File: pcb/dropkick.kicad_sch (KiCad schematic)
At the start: 50 parts, among them SW1 450405020524, SW2 KMR211NG_LFS, U1 ATSAMD21G18A-AUT, U2 SAM-M8Q-0-10, U3 MCP73831T-2ACI/OT, U4 DPS310XTSA1, U5 MPU-6050, U6 SPX3819-3.3, X1 microUSB, X2 JSTPH, X3 microsd, X5 32768Hz

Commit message: V3 board
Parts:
- removed JP4: HEADER-1X12, 1X12_ROUND, symbol Adafruit Feather M0 Adalogger-eagle-import:HEADER-1X12
- removed JP5: HEADER-1X16ROUND, 1X16_ROUND, symbol Adafruit Feather M0 Adalogger-eagle-import:HEADER-1X16ROUND
- removed R11: 4.7K, RESPACK_4X0603, symbol Adafruit MPU6050-eagle-import:RESISTOR_4PACK
- removed U2: SAM-M8Q-0-10, MODULE_SAM-M8Q-0-10, symbol dropkick:SAM-M8Q-0-10
- added J1: Conn_01x08, Connector_PinHeader_2.54mm:PinHeader_1x08_P2.54mm_Vertical, symbol Connector_Generic:Conn_01x08
- added R11, R12: 10K, Resistor_SMD:R_0603_1608Metric, symbol Adafruit MPU6050-eagle-import:RESISTOR_0603_NOOUT
- added R4, R5: 0K, Resistor_SMD:R_0603_1608Metric, symbol Adafruit Feather M0 Adalogger-eagle-import:RESISTOR_0603_NOOUT
- added U2: CAM-M8C-0, lib_fr:CAM-M8C-0, symbol dropkick:CAM-M8C-0
- added X4: ANTENNA_U.FL, lib_fr:U.FL, symbol Adafruit Ultimate GPS FeatherWing-eagle-import:ANTENNA_U.FL
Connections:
- net 3.3V is gone; now on net +3V3: C11.1, C6.1, R10.1, SJ4.1, U4.6 (VDDIO), U4.8 (VDD), U5.13 (VDD), U5.8 (VLOGIC)
- net VCC is gone; now on net +3V3: JP2.1
- net +3V3: now also R11.1, R12.1, U2.1 (VCC_IO), U2.9 (VCC)
- net A0: now also J1.6 (Pin_6)
- net A1: now also J1.7 (Pin_7)
- net AREF: now also J1.5 (Pin_5)
- net D0: now also J1.8 (Pin_8)
- net GND: now also J1.4 (Pin_4), U2.10 (GND), U2.11 (GND), U2.12 (GND), U2.13 (GND), U2.14 (GND), U2.15 (GND), U2.18 (GND), U2.19 (GND), U2.21 (GND), U2.22 (GND), U2.27 (GND), U2.31 (GND), U2.4 (GND), U2.5 (GND), X4.1 (GND@0), X4.2 (GND@1)
- net SCL: now also J1.2 (Pin_2), R11.2, U2.6 (SCL/_SPI_CLK)
- net SDA: now also J1.3 (Pin_3), R12.2, U2.3 (SDA/_SPI_CS_N)
- net VBACKUP: now also U2.8 (V_BCKP)
- net VBAT: now also J1.1 (Pin_1)
- new net: R4.2, R5.2, U2.17 (RF_IN)
- new net: R5.1, X4.3 (SIGNAL)
- new net RF: R4.1, U2.16 (RF_OUT)
- no-connect marks 21 -> 26
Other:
- note added: "GNSS RECEIVER - CAM-M8C"
- note removed: "GPS RECEIVER"
- moved on the sheet: B1, C11, TP1

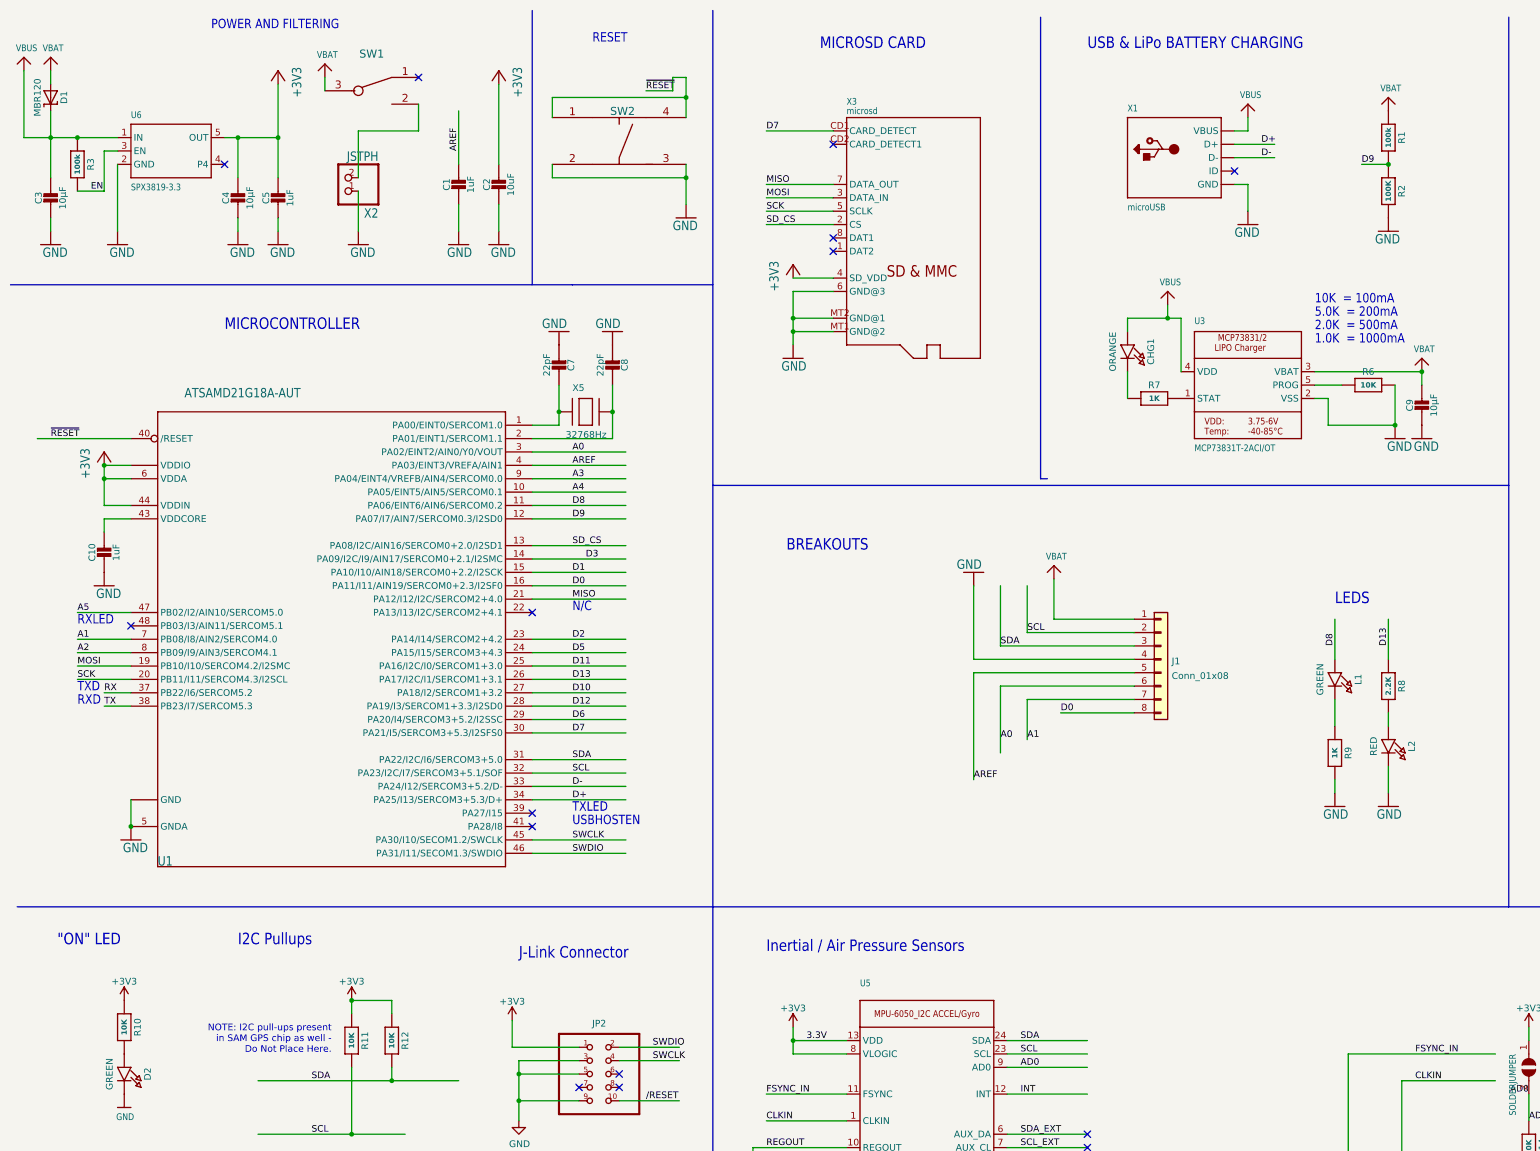
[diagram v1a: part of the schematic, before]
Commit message: Alternate REG IC
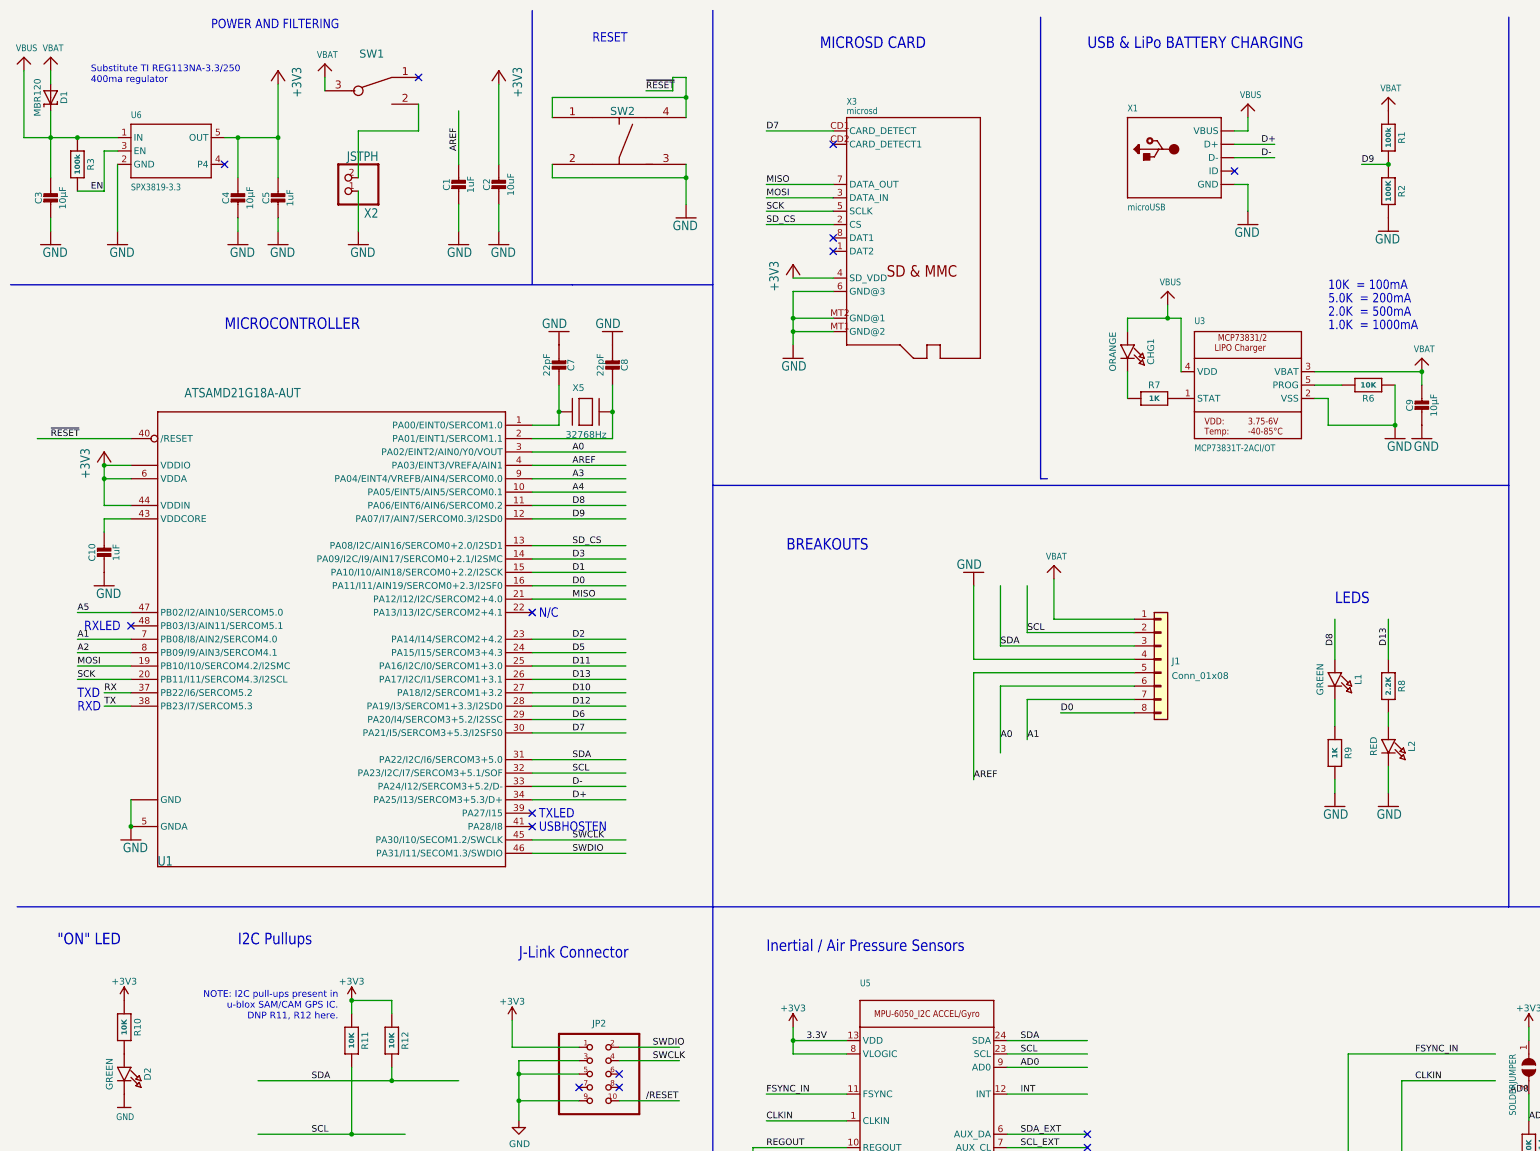
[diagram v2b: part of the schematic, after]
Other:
- note added: "NOTE: I2C pull-ups present in u-blox SAM/CAM GPS IC. DNP R11, R12 here."
- note added: "Substitute TI REG113NA-3.3/250 400ma regulator"
- note removed: "NOTE: I2C pull-ups present in SAM GPS chip as well - Do Not Place Here."
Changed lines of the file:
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@@
     (stroke (width 0) (type default) (color 0 0 0 0))
   )
-  (text "TXLED" (at 121.92 167.64 180)
-    (effects (font (size 1.778 1.5113)) (justify left bottom))
-  )
-  (text "TXD" (at 27.94 144.78 180)
+  (text "TXLED" (at 115.57 168.91 180)
+    (effects (font (size 1.778 1.5113)) (justify left bottom))
+  )
+  (text "TXD" (at 27.94 146.05 180)
     (effects (font (size 1.778 1.5113)) (justify left bottom))
   )
@@
     (effects (font (size 2.1844 1.8567)) (justify left bottom))
   )
-  (text "USBHOSTEN" (at 121.92 170.18 180)
-    (effects (font (size 1.778 1.5113)) (justify left bottom))
-  )
-  (text "RXD" (at 27.94 147.32 180)
-    (effects (font (size 1.778 1.5113)) (justify left bottom))
-  )
-  (text "N/C" (at 121.92 129.54 180)
+  (text "USBHOSTEN" (at 115.57 171.45 180)
+    (effects (font (size 1.778 1.5113)) (justify left bottom))
+  )
+  (text "RXD" (at 27.94 148.59 180)
+    (effects (font (size 1.778 1.5113)) (justify left bottom))
+  )
+  (text "N/C" (at 115.57 130.81 180)
     (effects (font (size 1.778 1.5113)) (justify left bottom))
   )
@@
     (effects (font (size 2.1844 1.8567)) (justify left bottom))
   )
-  (text "10K  = 100mA" (at 262.89 71.12 180)
+  (text "10K  = 100mA" (at 265.43 68.58 180)
     (effects (font (size 1.778 1.5113)) (justify left bottom))
   )
@@
     (effects (font (size 2.1844 1.8567)) (justify left bottom))
   )
-  (text "1.0K  = 1000mA" (at 262.89 78.74 180)
-    (effects (font (size 1.778 1.5113)) (justify left bottom))
-  )
-  (text "5.0K  = 200mA" (at 262.89 73.66 180)
+  (text "1.0K  = 1000mA" (at 265.43 76.2 180)
+    (effects (font (size 1.778 1.5113)) (justify left bottom))
+  )
+  (text "5.0K  = 200mA" (at 265.43 71.12 180)
     (effects (font (size 1.778 1.5113)) (justify left bottom))
   )
@@
     (effects (font (size 2.1844 1.8567)) (justify left bottom))
   )
-  (text "RXLED" (at 27.94 132.08 180)
-    (effects (font (size 1.778 1.5113)) (justify left bottom))
+  (text "RXLED" (at 29.21 133.35 180)
+    (effects (font (size 1.778 1.5113)) (justify left bottom))
+  )
+  (text "Substitute TI REG113NA-3.3/250\n400ma regulator\n" (at 30.48 29.21 0)
+    (effects (font (size 1.27 1.27)) (justify left bottom))
   )
   (text "LEDS" (at 266.7 128.27 180)
     (effects (font (size 2.1844 1.8567)) (justify left bottom))
   )
-  (text "2.0K  = 500mA" (at 262.89 76.2 180)
+  (text "2.0K  = 500mA" (at 265.43 73.66 180)
     (effects (font (size 1.778 1.5113)) (justify left bottom))
   )
@@
     (effects (font (size 2.1844 1.8567)) (justify left bottom))
   )
-  (text "NOTE: I2C pull-ups present\nin SAM GPS chip as well - \nDo Not Place Here."
-    (at 76.2 213.36 0)
+  (text "NOTE: I2C pull-ups present in\nu-blox SAM/CAM GPS IC.\nDNP R11, R12 here."
+    (at 77.47 207.01 0)
     (effects (font (size 1.27 1.27)) (justify right bottom))
   )
-  (label "D3" (at 124.46 119.38 0)
+  (label "D3" (at 121.92 119.38 0)
     (effects (font (size 1.2446 1.2446)) (justify left bottom))
   )
@@
   (symbol (lib_id "Adafruit Feather M0 Adalogger-eagle-import:RESISTOR_0603_NOOUT") (at 273.05 86.36 0) (unit 1)
     (in_bom yes) (on_board yes)
-    (property "Reference" "R6" (id 0) (at 273.05 83.82 0))
+    (property "Reference" "R6" (id 0) (at 273.05 88.9 0))
     (property "Value" "10K" (id 1) (at 273.05 86.36 0)
       (effects (font (size 1.016 1.016) bold))
@@
       (effects (font (size 1.27 1.27)) hide)
     )
-    (property "Datasheet" "" (id 3) (at 250.19 86.36 0)
+    (property "Datasheet" "https://www.mouser.com/datasheet/2/268/MCHP_S_A0010728890_1-2521060.pdf" (id 3) (at 250.19 86.36 0)
       (effects (font (size 1.27 1.27)) hide)
     )
@@
       (effects (font (size 1.27 1.27)) hide)
     )
-    (property "Datasheet" "" (id 3) (at 45.72 41.91 0)
-      (effects (font (size 1.27 1.27)) hide)
-    )
+    (property "Datasheet" "https://assets.maxlinear.com/web/documents/spx3819.pdf" (id 3) (at 45.72 41.91 0)
+      (effects (font (size 1.27 1.27)) hide)
+    )

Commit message: IC substitutions
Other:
- note added: "Sub B0540W-7-F"
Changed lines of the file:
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@@
     (effects (font (size 1.27 1.27)) (justify right bottom))
+  )
+  (text "Sub B0540W-7-F" (at 15.24 44.45 90)
+    (effects (font (size 1.27 1.27)) (justify left bottom))
   )
   (label "D3" (at 121.92 119.38 0)

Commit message: Reorganize footprint libraries
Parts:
- C12, C13: footprint 0603-NO -> Capacitor_SMD:C_0603_1608Metric
- R1, R3: value 100k -> 100K; footprint 0603-NO -> Resistor_SMD:R_0603_1608Metric
- R2: footprint 0603-NO -> Resistor_SMD:R_0603_1608Metric
- SJ4: footprint 310:0603-NO -> Resistor_SMD:R_0603_1608Metric
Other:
- note added: "EXT"
- note added: "INT"
- note added: "Install one of INT (R4) or EXT (R5) jumper"
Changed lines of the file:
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@@
     (stroke (width 0) (type default) (color 0 0 0 0))
+  )
+  (text "Install one of INT (R4) or \nEXT (R5) jumper" (at 325.12 88.9 0)
+    (effects (font (size 1.27 1.27)) (justify left bottom))
   )
   (text "TXLED" (at 115.57 168.91 180)
@@
     (effects (font (size 1.778 1.5113)) (justify left bottom))
   )
+  (text "INT" (at 334.01 93.98 0)
+    (effects (font (size 1.27 1.27)) (justify left bottom))
+  )
   (text "Inertial / Air Pressure Sensors" (at 158.75 194.31 180)
     (effects (font (size 2.1844 1.8567)) (justify left bottom))
@@
   (text "5.0K  = 200mA" (at 265.43 71.12 180)
     (effects (font (size 1.778 1.5113)) (justify left bottom))
+  )
+  (text "EXT" (at 334.01 104.14 0)
+    (effects (font (size 1.27 1.27)) (justify left bottom))
   )
   (text "BREAKOUTS" (at 162.56 118.11 180)
@@
       (effects (font (size 1.27 1.0795)) (justify left bottom))
     )
-    (property "Footprint" "310:0603-NO" (id 2) (at 303.53 215.9 0)
+    (property "Footprint" "Resistor_SMD:R_0603_1608Metric" (id 2) (at 303.53 215.9 0)
       (effects (font (size 1.27 1.27)) hide)
     )
@@
     (property "Reference" "C12" (id 0) (at 153.92 240.05 90))
     (property "Value" "0.1uF" (id 1) (at 158.51 240.05 90))
-    (property "Footprint" "0603-NO" (id 2) (at 156.21 241.3 0)
+    (property "Footprint" "Capacitor_SMD:C_0603_1608Metric" (id 2) (at 156.21 241.3 0)
       (effects (font (size 1.27 1.27)) hide)
     )
@@
       (effects (font (size 1.016 1.016) bold))
     )
-    (property "Footprint" "0603-NO" (id 2) (at 276.86 49.53 0)
+    (property "Footprint" "Resistor_SMD:R_0603_1608Metric" (id 2) (at 276.86 49.53 0)
       (effects (font (size 1.27 1.27)) hide)
     )
@@
     (in_bom yes) (on_board yes)
     (property "Reference" "R1" (id 0) (at 279.4 39.37 0))
-    (property "Value" "100k" (id 1) (at 276.86 39.37 0)
+    (property "Value" "100K" (id 1) (at 276.86 39.37 0)
       (effects (font (size 1.016 1.016) bold))
     )
-    (property "Footprint" "0603-NO" (id 2) (at 276.86 39.37 0)
+    (property "Footprint" "Resistor_SMD:R_0603_1608Metric" (id 2) (at 276.86 39.37 0)
       (effects (font (size 1.27 1.27)) hide)
     )
@@
     (property "Reference" "C13" (id 0) (at 161.54 240.05 90))
     (property "Value" "2.2nF" (id 1) (at 166.13 240.05 90))
-    (property "Footprint" "0603-NO" (id 2) (at 163.83 241.3 0)
+    (property "Footprint" "Capacitor_SMD:C_0603_1608Metric" (id 2) (at 163.83 241.3 0)
       (effects (font (size 1.27 1.27)) hide)
     )
@@
     (in_bom yes) (on_board yes)
     (property "Reference" "R3" (id 0) (at 30.48 44.45 0))
-    (property "Value" "100k" (id 1) (at 27.94 44.45 0)
+    (property "Value" "100K" (id 1) (at 27.94 44.45 0)
       (effects (font (size 1.016 1.016) bold))
     )
-    (property "Footprint" "0603-NO" (id 2) (at 27.94 44.45 0)
+    (property "Footprint" "Resistor_SMD:R_0603_1608Metric" (id 2) (at 27.94 44.45 0)
       (effects (font (size 1.27 1.27)) hide)
     )
@@
     )
     (path "/265c9ea2-10c9-4dc4-a415-1a2555e54dd9"
-      (reference "C12") (unit 1) (value "0.1uF") (footprint "0603-NO")
+      (reference "C12") (unit 1) (value "0.1uF") (footprint "Capacitor_SMD:C_0603_1608Metric")
     )
     (path "/eab08a4f-1a64-481f-b898-2169bbdf568b"
-      (reference "C13") (unit 1) (value "2.2nF") (footprint "0603-NO")
+      (reference "C13") (unit 1) (value "2.2nF") (footprint "Capacitor_SMD:C_0603_1608Metric")
     )
     (path "/3c5c540c-f2b8-43e0-a682-33d4cb1f2236"
@@
     )
     (path "/cd4c9a58-7d08-4935-96d2-a2f0e9d7a216"
-      (reference "R1") (unit 1) (value "100k") (footprint "0603-NO")
+      (reference "R1") (unit 1) (value "100K") (footprint "Resistor_SMD:R_0603_1608Metric")
     )
     (path "/64ec41fa-ed2b-40b9-a2b5-ea88e5ab79cc"
-      (reference "R2") (unit 1) (value "100K") (footprint "0603-NO")
+      (reference "R2") (unit 1) (value "100K") (footprint "Resistor_SMD:R_0603_1608Metric")
     )
     (path "/f883267e-e7c9-40c1-96cb-d827ca2e14b4"
-      (reference "R3") (unit 1) (value "100k") (footprint "0603-NO")
+      (reference "R3") (unit 1) (value "100K") (footprint "Resistor_SMD:R_0603_1608Metric")
     )
     (path "/75e84725-7201-4c50-b1a0-88e3a30903e4"
@@
     )
     (path "/1d41875d-8419-4731-9a57-168ae69c4de4"
-      (reference "SJ4") (unit 1) (value "SOLDERJUMPER") (footprint "310:0603-NO")
+      (reference "SJ4") (unit 1) (value "SOLDERJUMPER") (footprint "Resistor_SMD:R_0603_1608Metric")
     )
     (path "/92bef28d-c11f-4149-ae27-34f9e91c5fec"

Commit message: Add BOM, minor footprint fixes
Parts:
- JP2: footprint logger:3221-10-0300-00-TR -> lib_fp:3221-10-0300-00-TR
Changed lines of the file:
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@@
       (effects (font (size 1.27 1.27)) hide)
     )
-    (property "Footprint" "logger:3221-10-0300-00-TR" (id 2) (at 125.73 217.17 0)
+    (property "Footprint" "lib_fp:3221-10-0300-00-TR" (id 2) (at 125.73 217.17 0)
       (effects (font (size 1.27 1.27)) (justify left bottom) hide)
     )
@@
     )
     (path "/de4ebb72-f6e1-42e1-acf2-16277a14855f"
-      (reference "JP2") (unit 1) (value "3221-10-0300-00-TR") (footprint "logger:3221-10-0300-00-TR")
+      (reference "JP2") (unit 1) (value "3221-10-0300-00-TR") (footprint "lib_fp:3221-10-0300-00-TR")
     )
     (path "/d777be5d-c510-4a8d-bd61-5cfa760360b6"

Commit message: Tweak BOM, add MFR part numbers
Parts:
- B1: Manufacturer Part (none) -> 1056TR
- C1, C10, C5: value 1uF -> 1µF
- C11, C2: value 10uF -> 10µF; Manufacturer Part (none) -> C0805C106K8RACTU
- C12, C6: value 0.1uF -> 0.1µF; Manufacturer Part (none) -> VJ0603Y104JXXAC
- C13: Manufacturer Part (none) -> C0603C222K1HACAUTO
- C3, C4, C9: Manufacturer Part (none) -> C0805C106K8RACTU
- C7, C8: Manufacturer Part (none) -> 06035U220FAT2A
- CHG1: value ORANGE -> ORANGE LED; Manufacturer Part (none) -> AA1112H-TR
- D1: Manufacturer Part (none) -> PMEG2005EGWX
- D2, L1: value GREEN -> GREEN LED; Manufacturer Part (none) -> LTST-S270KGKT
- H1, H2, H3, H4: footprint logger:MOUNTINGHOLE_2.5_PLATED -> lib_fp:MOUNTINGHOLE_2.5_PLATED; now left out of the parts list
- JP2: Manufacturer Part (none) -> 3221-10-0300-00-TR
- L2: value RED -> RED LED; Manufacturer Part (none) -> LTST-S270KRKT
- R1, R2, R3: Manufacturer Part (none) -> TNPW0603100KBEEA
- R10, R11, R12, R14, R6: Comments (none) -> R11-R12 DNP
- R4, R5: Comments (none) -> Select one only
- R8: Manufacturer Part (none) -> CRCW06032K20FKEAHP
- SW1: footprint logger:450405020524 -> lib_fp:450405020524; Manufacturer Part (none) -> 450405020524
- SW2: footprint logger:KMR211NG LFS -> lib_fp:KMR211NG LFS; Manufacturer Part (none) -> KMR211NG LFS
- TP1: now left out of the parts list
- U1: value ATSAMD21G18A-AUT -> ATSAMD21G18A-AUT; footprint logger:ATSAMD21G15B-AU -> lib_fp:ATSAMD21G15B-AU; Manufacturer Part (none) -> ATSAMD21G18A-AUT
- U2: Manufacturer Part (none) -> CAM-M8C-0
- U3: Manufacturer Part (none) -> MCP73831T-2ACI/OT
- U4: footprint logger:DPS310XTSA1 -> lib_fp:DPS310XTSA1; Manufacturer Part (none) -> DPS310XTSA1
- U5: Manufacturer Part (none) -> MPU-6050
- U6: Manufacturer Part (none) -> SPX3819M5-L-3-3/TR
- X1: value microUSB -> USB micro-B; Manufacturer Part (none) -> 4UCONN_20329_V2
- X3: Manufacturer Part (none) -> MEM2061-01-188-00-A
- X4: Manufacturer Part (none) -> U.FL-R-SMT(10)
- X5: Manufacturer Part (none) -> FC-135 32.7680KA-A5

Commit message: V4 board candidate
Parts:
- removed J1: Conn_01x08, Connector_PinHeader_2.54mm:PinHeader_1x08_P2.54mm_Vertical, symbol Connector_Generic:Conn_01x08
- added J1: Conn_01x10, Connector_PinSocket_2.54mm:PinSocket_1x10_P2.54mm_Vertical, symbol Connector_Generic:Conn_01x10
- added R13, R15: 200, Resistor_SMD:R_0603_1608Metric, symbol Adafruit Feather M0 Adalogger-eagle-import:RESISTOR_0603_NOOUT
- CHG1, L1, L2: footprint CHIPLED_0805_NOOUTLINE -> LED_SMD:LED_0603_1608Metric
- D2: footprint CHIPLED_0603_NOOUTLINE -> LED_SMD:LED_0603_1608Metric
- U2: footprint lib_fr:CAM-M8C-0 -> lib_fp:CAM-M8C-0
- X4: footprint lib_fr:U.FL -> lib_fp:U.FL
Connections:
- net +3V3: now also J1.2 (Pin_2)
- net A0: now also J1.7 (Pin_7)
- net A1: now also J1.8 (Pin_8)
- net AREF: now also J1.6 (Pin_6)
- net D0: now also J1.9 (Pin_9), R13.1
- net D1: now also J1.10 (Pin_10), R15.1
- net GND: now also J1.5 (Pin_5)
- net SCL: now also J1.3 (Pin_3)
- net SDA: now also J1.4 (Pin_4)
- net VBAT: now also J1.1 (Pin_1)
- net at U2.25 (TXD/_SPI_MISO): now also R13.2
- net at U2.26 (RXD/_SPI_MOSI): now also R15.2
- net RX: no longer names the net of U1.37 (PB22/I6/SERCOM5.2)
- net TX: no longer names the net of U1.38 (PB23/I7/SERCOM5.3)
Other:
- note added: "RX"
- note added: "TX"
- note removed: "RXD"
- note removed: "RXLED"
- note removed: "TXD"
- note removed: "TXLED"
- note removed: "USBHOSTEN"
